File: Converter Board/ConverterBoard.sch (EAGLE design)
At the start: 18 parts

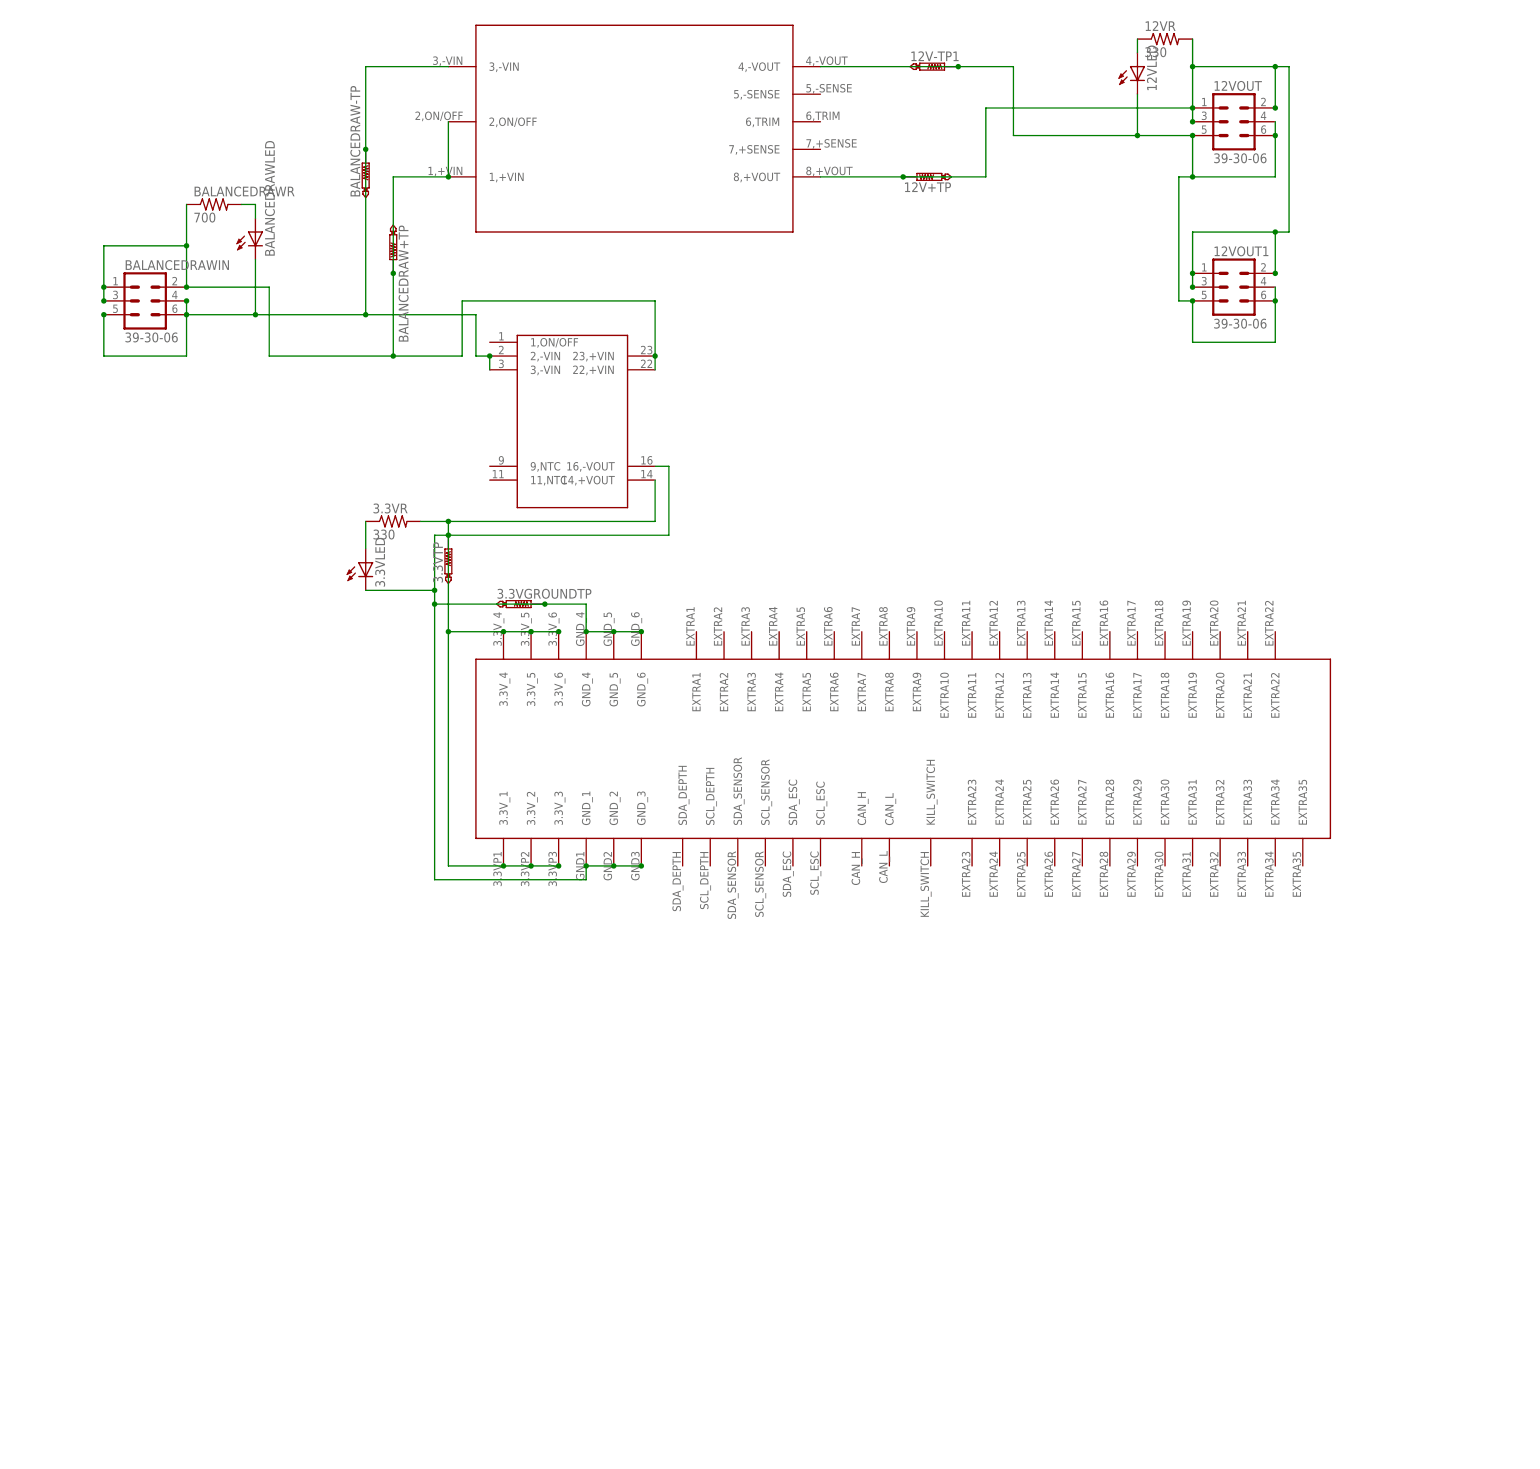
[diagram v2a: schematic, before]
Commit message: Cleaned and updated converter board, added spots for capacitors
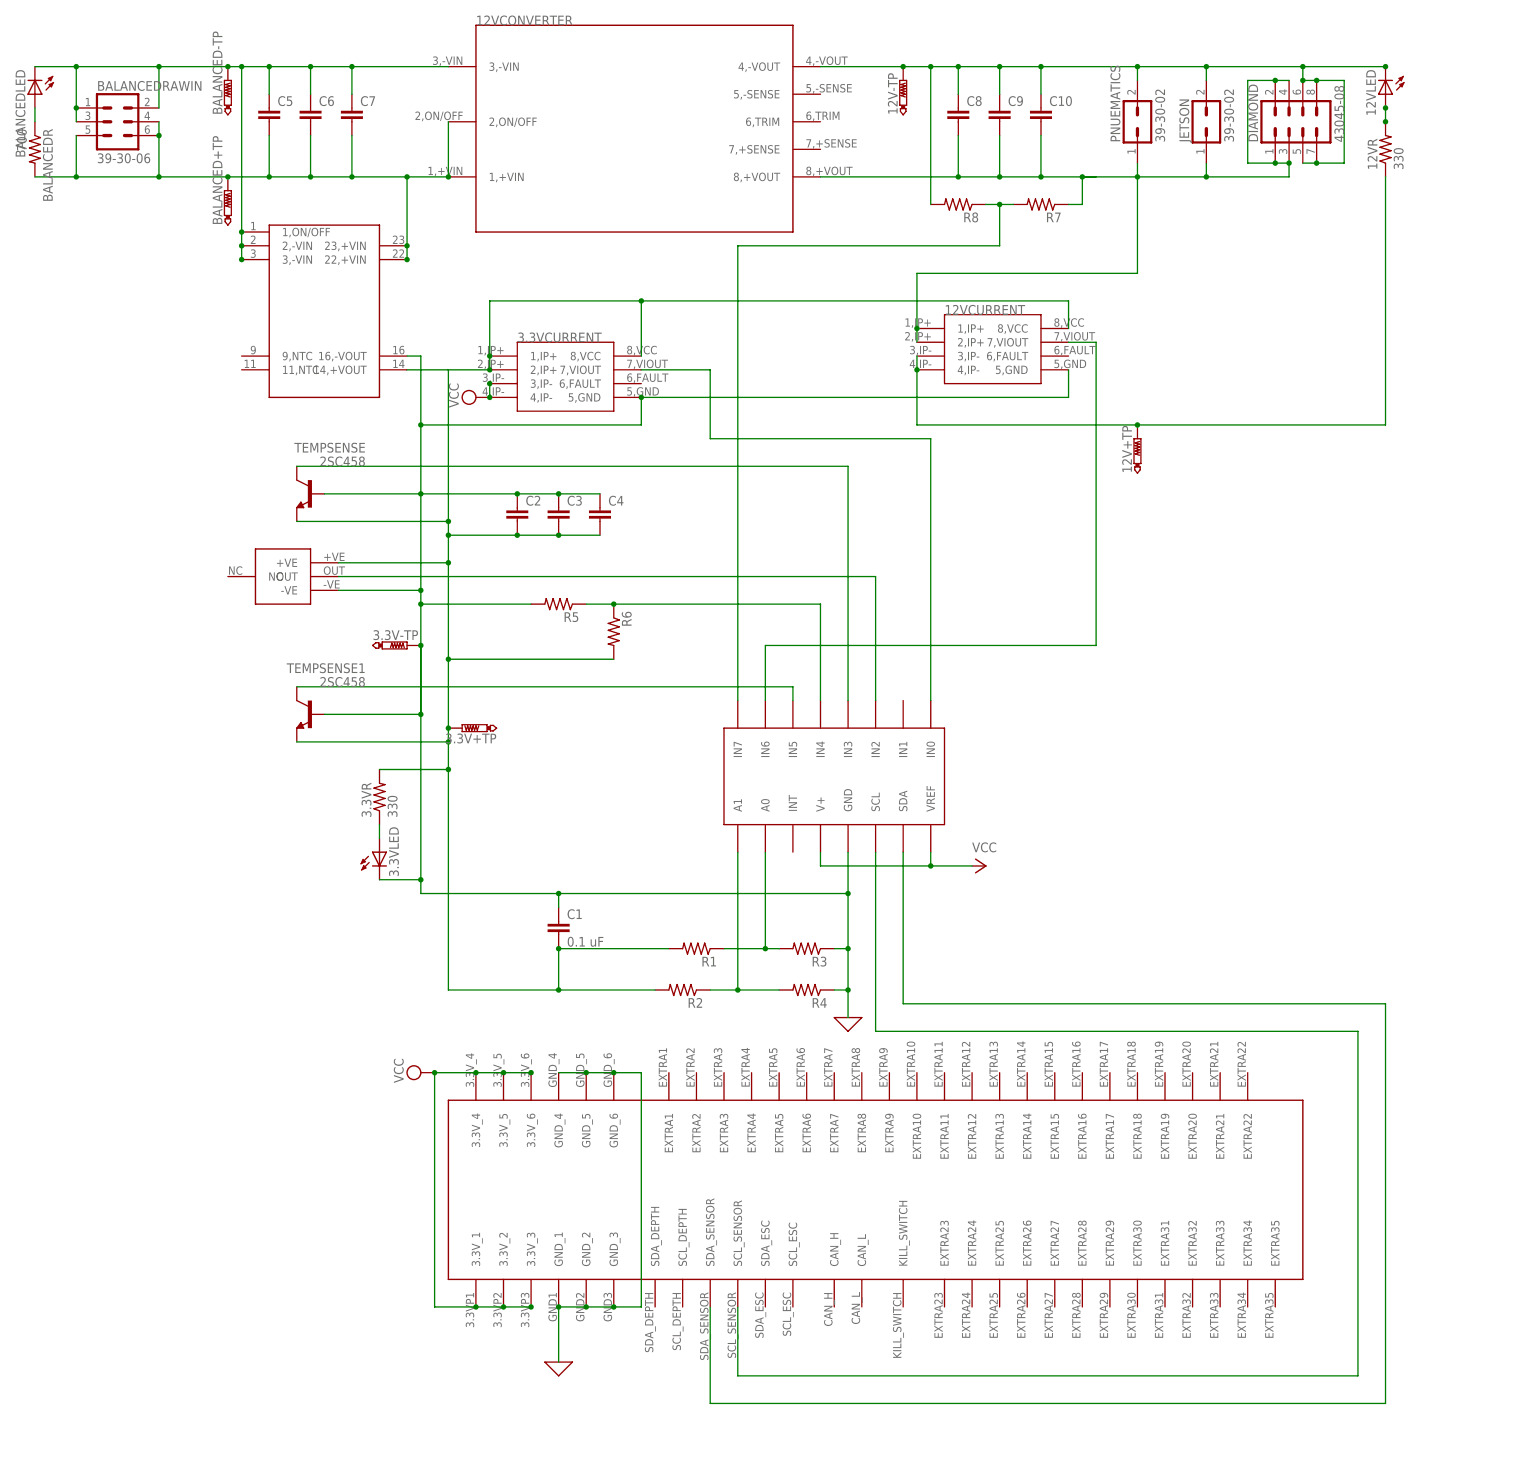
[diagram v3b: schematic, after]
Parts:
- removed 12V-TP1, 3.3VGROUNDTP, 3.3VTP, BALANCEDRAW+TP, BALANCEDRAW-TP: PTR1B1,27, testpad:PTR1B1,27
- removed 12VOUT, 12VOUT1: 39-30-06, con-molex-mini-fit:39-30-06
- removed BALANCEDRAWLED: LTST-S270GKT, LTST-S270GKT:LTST-S270GKT
- removed BALANCEDRAWR: 700, resistor:R-US_0204/7
- added 12V-TP, 3.3V+TP, 3.3V-TP, BALANCED+TP, BALANCED-TP: PTR1B1,27, testpad:PTR1B1,27
- added 12VCURRENT, 3.3VCURRENT: CURRENTSENS, CurrentSensor:CURRENTSENS
- added BALANCEDLED: LTST-S270GKT, LTST-S270GKT:LTST-S270GKT
- added BALANCEDR: 700, resistor:R-US_0204/7
- added C1: 0.1 uF, resistor:C-EU025-024X044
- added C10, C2, C3, C4, C5, C6, C7, C8, C9: (no value), resistor:C-EU025-024X044
- added DIAMOND: 43045-08, con-molex-micro-fit:43045-08
- added JETSON, PNUEMATICS: 39-30-02, con-molex-mini-fit:39-30-02
- added R1, R2, R3, R4, R5, R6, R7, R8: (no value), resistor:R-US_0204/7
- added TEMPSENSE, TEMPSENSE1: 2SC458, transistor:2SC458
- added U$6: HUMIDITYSENSOR, HumiditySensor:HUMIDITYSENSOR
- added U$8: ADC128D818, ADC128D818:ADC128D818
- renumbered U$1 to 12VCONVERTER
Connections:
- removed net 12V+: 12V+TP.TP, 12VCONVERTER.8,+VOUT, 12VOUT.1, 12VOUT.2, 12VOUT.3, 12VOUT1.1, 12VOUT1.2, 12VOUT1.3, 12VR.2
- removed net 12V-: 12V-TP1.TP, 12VCONVERTER.4,-VOUT, 12VLED.C, 12VOUT.4, 12VOUT.5, 12VOUT.6, 12VOUT1.4, 12VOUT1.5, 12VOUT1.6
- removed net 3.3V: 3.3VR.2, 3.3VTP.TP, U$2.14,+VOUT, U$3.3.3V_1, U$3.3.3V_2, U$3.3.3V_3, U$3.3.3V_4, U$3.3.3V_5, U$3.3.3V_6
- removed net 3.3VGROUND: 3.3VGROUNDTP.TP, 3.3VLED.C, U$2.16,-VOUT, U$3.GND_1, U$3.GND_2, U$3.GND_3, U$3.GND_4, U$3.GND_5, U$3.GND_6
- removed net BALANCEDRAW+: 12VCONVERTER.1,+VIN, 12VCONVERTER.2,ON/OFF, BALANCEDRAW+TP.TP, BALANCEDRAWIN.1, BALANCEDRAWIN.2, BALANCEDRAWIN.3, BALANCEDRAWR.1, U$2.22,+VIN, U$2.23,+VIN
- removed net BALANCEDRAW-: 12VCONVERTER.3,-VIN, BALANCEDRAW-TP.TP, BALANCEDRAWIN.4, BALANCEDRAWIN.5, BALANCEDRAWIN.6, BALANCEDRAWLED.C, U$2.2,-VIN, U$2.3,-VIN
- removed net BALANCEDRAWLED: BALANCEDRAWLED.A, BALANCEDRAWR.2
- new net 12IDATA: 12VCURRENT.7,VIOUT, U$8.IN6
- new net 12VDATA: R7.2, R8.1, U$8.IN7
- new net 12VGND: 12V-TP.TP, 12VCONVERTER.4,-VOUT, 12VLED.C, C10.1, C8.1, C9.1, DIAMOND.5, DIAMOND.6, DIAMOND.7, DIAMOND.8, JETSON.2, PNUEMATICS.2, R8.2
- new net 12VMON: 12V+TP.TP, 12VCURRENT.3,IP-, 12VCURRENT.4,IP-, 12VR.1
- new net 12VUNMON: 12VCONVERTER.8,+VOUT, 12VCURRENT.1,IP+, 12VCURRENT.2,IP+, C10.2, C8.2, C9.2, DIAMOND.1, DIAMOND.2, DIAMOND.3, DIAMOND.4, JETSON.1, PNUEMATICS.1, R7.1
- new net 3.3IDATA: 3.3VCURRENT.7,VIOUT, U$8.IN0
- new net 3.3V+: 12VCURRENT.8,VCC, 3.3V+TP.TP, 3.3VCURRENT.1,IP+, 3.3VCURRENT.2,IP+, 3.3VCURRENT.8,VCC, 3.3VR.2, C1.2, C2.2, C3.2, C4.2, R1.2, R2.2, R6.2, TEMPSENSE.E, TEMPSENSE1.E, U$2.14,+VOUT, U$6.+VE
- new net 3.3VDATA: R5.1, R6.1, U$8.IN4
- new net 3.3VGND: 12VCURRENT.5,GND, 3.3V-TP.TP, 3.3VCURRENT.5,GND, 3.3VLED.C, C1.1, C2.1, C3.1, C4.1, R3.1, R4.1, R5.2, TEMPSENSE.B, TEMPSENSE1.B, U$2.16,-VOUT, U$3.GND_1, U$3.GND_2, U$3.GND_3, U$3.GND_4, U$3.GND_5, U$3.GND_6, U$6.-VE, U$8.GND
- new net A0: R1.1, R3.2, U$8.A0
- new net A1: R2.1, R4.2, U$8.A1
- new net BALANCED+: 12VCONVERTER.1,+VIN, 12VCONVERTER.2,ON/OFF, BALANCED+TP.TP, BALANCEDR.2, BALANCEDRAWIN.4, BALANCEDRAWIN.5, BALANCEDRAWIN.6, C5.2, C6.2, C7.2, U$2.22,+VIN, U$2.23,+VIN
- new net BALANCEDGND: 12VCONVERTER.3,-VIN, BALANCED-TP.TP, BALANCEDLED.C, BALANCEDRAWIN.1, BALANCEDRAWIN.2, BALANCEDRAWIN.3, C5.1, C6.1, C7.1, U$2.1,ON/OFF, U$2.2,-VIN, U$2.3,-VIN
- new net BALANCEDLED: BALANCEDLED.A, BALANCEDR.1
- new net HUMIDITYDATA: U$6.OUT, U$8.IN2
- new net SCL: U$3.SCL_SENSOR, U$8.SCL
- new net SDA: U$3.SDA_SENSOR, U$8.SDA
- new net TEMP1DATA: TEMPSENSE1.C, U$8.IN5
- new net TEMPDATA: TEMPSENSE.C, U$8.IN3
- new net VCC: 3.3VCURRENT.3,IP-, 3.3VCURRENT.4,IP-, U$3.3.3V_1, U$3.3.3V_2, U$3.3.3V_3, U$3.3.3V_4, U$3.3.3V_5, U$3.3.3V_6, U$8.V+, U$8.VREF
- net 12VLED: now also 12VR.2; no longer 12VR.1
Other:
- moved on the sheet: 12V+TP, 12VLED, 12VR, 3.3VLED, 3.3VR, BALANCEDRAWIN

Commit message: Added correct capacitors, rearranged parts
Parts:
- removed C2, C3, C4: (no value), resistor:C-EU025-024X044
- C10, C8: value (none) -> 1uF
- C5, C6: value (none) -> 1000pF
- C7: value (none) -> 220uF
- C9: value (none) -> 10uF
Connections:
- removed net 12VGND: 12V-TP.TP, 12VCONVERTER.4,-VOUT, 12VLED.C, C10.1, C8.1, C9.1, DIAMOND.5, DIAMOND.6, DIAMOND.7, DIAMOND.8, JETSON.2, PNUEMATICS.2, R8.2
- removed net 12VMON: 12V+TP.TP, 12VCURRENT.3,IP-, 12VCURRENT.4,IP-, 12VR.1
- removed net 12VUNMON: 12VCONVERTER.8,+VOUT, 12VCURRENT.1,IP+, 12VCURRENT.2,IP+, C10.2, C8.2, C9.2, DIAMOND.1, DIAMOND.2, DIAMOND.3, DIAMOND.4, JETSON.1, PNUEMATICS.1, R7.1
- new net 12V+: 12V+TP.TP, 12VCONVERTER.7,+SENSE, 12VCONVERTER.8,+VOUT, C10.1, C9.1
- new net 12VCIN: 12VCONVERTER.1,+VIN, 12VCONVERTER.2,ON/OFF, 12VCURRENT.1,IP+, 12VCURRENT.2,IP+, BALANCED+TP.TP, BALANCEDR.2, C10.2, C7.1, C9.2, R7.1
- new net 12VCOUT: 12VCURRENT.3,IP-, 12VCURRENT.4,IP-, 12VR.1, DIAMOND.1, DIAMOND.2, DIAMOND.3, DIAMOND.4, JETSON.1, PNUEMATICS.1
- new net 3.3VC: C6.1, C8.2, U$2.22,+VIN, U$2.23,+VIN
- new net GND: 12V-TP.TP, 12VCONVERTER.4,-VOUT, 12VCONVERTER.5,-SENSE, 12VCURRENT.5,GND, 12VLED.C, 3.3V-TP.TP, 3.3VCURRENT.5,GND, 3.3VLED.C, C1.1, C5.2, DIAMOND.5, DIAMOND.6, DIAMOND.7, DIAMOND.8, JETSON.2, PNUEMATICS.2, R3.1, R4.1, R5.2, R8.2, TEMPSENSE.B, TEMPSENSE1.B, U$2.16,-VOUT, U$6.-VE, U$8.GND
- net 3.3V+: now also C6.2; no longer C2.2, C3.2, C4.2
- net 3.3VGND: no longer 12VCURRENT.5,GND, 3.3V-TP.TP, 3.3VCURRENT.5,GND, 3.3VLED.C, C1.1, C2.1, C3.1, C4.1, R3.1, R4.1, R5.2, TEMPSENSE.B, TEMPSENSE1.B, U$2.16,-VOUT, U$6.-VE, U$8.GND
- net BALANCED+: now also C8.1; no longer 12VCONVERTER.1,+VIN, 12VCONVERTER.2,ON/OFF, BALANCED+TP.TP, BALANCEDR.2, C5.2, C6.2, U$2.22,+VIN, U$2.23,+VIN
- net BALANCEDGND: no longer C6.1, C7.1
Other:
- moved on the sheet: 12V+TP, 12VCONVERTER, 12VCURRENT, BALANCED+TP, BALANCEDLED, BALANCEDR, C10, C5, C6, C7, C8, C9
